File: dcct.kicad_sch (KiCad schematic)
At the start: 0 parts

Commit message: Add DCCT ADCs
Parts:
- added C147, C153, C154, C155, C156, C157, C160, C161, C162, C166, C171, C172, C178, C180: 10uF, Capacitor_SMD:C_0603_1608Metric, symbol Device:C_Small
- added C148, C152, C158, C163, C164, C165, C170, C173, C174, C179, C181: 0.1uF, Capacitor_SMD:C_0402_1005Metric, symbol Device:C_Small
- added C149, C150, C167, C169, C175, C177: 6800pF, Capacitor_SMD:C_0402_1005Metric, symbol Device:C_Small
- added C151, C168, C176: 3300pF, Capacitor_SMD:C_0402_1005Metric, symbol Device:C_Small
- added C159: 0.01uF, Capacitor_SMD:C_0402_1005Metric, symbol Device:C_Small
- added R54, R55: 1.0K, Resistor_SMD:R_0402_1005Metric, symbol Device:R_US
- added R56: 665, Resistor_SMD:R_0402_1005Metric, symbol Device:R_US
- added R57: 0, Resistor_SMD:R_0402_1005Metric, symbol Device:R_US
- added R58: 1.3K, Resistor_SMD:R_0402_1005Metric, symbol Device:R_US
- added R59, R60: 10K, Resistor_SMD:R_0402_1005Metric, symbol Device:R_US
- added R61, R62: 10, Resistor_SMD:R_0402_1005Metric, symbol Device:R_US
- added R63: 15, Resistor_SMD:R_0402_1005Metric, symbol Device:R_US
- added R64, R65: 30.1, Resistor_SMD:R_0402_1005Metric, symbol Device:R_US
- added U32: LTC6655BHLS8-5, myparts:LTC6655, symbol PSC:LTC6655BHLS8-5
- added U33: AD8429BRZ, myparts:SOIC127P600X175-8N, symbol Amplifier_Instrumentation:AD8429BRZ
- added U34: AD8675ARZ, Package_SO:SOIC-8_3.9x4.9mm_P1.27mm, symbol PSC:AD8675ARZ
- added U35: LT6202CS5, myparts:LT6202CS5, symbol PSC:LT6202CS5
- added U36: LTC6363xMS8, Package_SO:MSOP-8_3x3mm_P0.65mm, symbol PSC:LTC6363xMS8
- added U37: LTC2376CDE-20-PBF, DFN-16_DE_LIT, symbol PSC:LTC2376CDE-20-PBF
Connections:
- new net: C176.2, C177.1, R65.1, U37.4 (IN+)
- new net: R65.2, U36.4 (+)
- new net: C160.1, R59.1, R60.1, U35.3 (+)
- new net: C168.2, C169.1, R63.1, U36.1 (-)
- new net: C166.1, C170.1, R61.1, U36.2 (VOCM)
- new net: R64.2, U36.5 (-)
- new net: C167.2, C168.1, R62.1, U36.8 (+)
- new net: C155.1, C157.1, R57.1, R59.2, U37.7 (REF), U37.8 (REF/*DGC)
- new net: C153.1, R57.2, U32.6 (VOUT_S), U32.7 (VOUT_F)
- new net: R61.2, U35.1, U35.4 (-)
- new net: R62.2, U34.2 (-), U34.6
- new net: C159.1, R58.1, U34.3 (+)
- new net: C175.2, C176.1, R64.1, U37.5 (IN-)
- new net: C149.2, C151.1, R54.1, U33.1 (-)
- new net: C150.1, C151.2, R55.1, U33.4 (+)
- new net: R58.2, U33.7
- new net: R56.1, U33.2 (Rg)
- new net: R56.2, U33.3 (Rg)
- new net +1.8V: C180.1, C181.1, U37.15 (OVDD)
- new net +10V: C147.1, C148.1, U32.1 (IN), U32.2 (~SHDN)
- new net +15V: C156.1, C158.1, C162.1, C165.1, U33.8 (Vs+), U34.7 (V+)
- new net +2.5V: C178.1, C179.1, U37.2 (VDD)
- new net +5.3VA: C164.1, C171.1, C173.1, U35.5 (V+), U36.3 (V+)
- new net -15V: C152.1, C154.1, C161.1, C163.1, U33.5 (Vs-), U34.4 (V-)
- new net -5.3VA: C172.1, C174.1, U36.6 (V-)
- new net GND: C147.2, C148.2, C149.1, C150.2, C152.2, C153.2, C154.2, C155.2, C156.2, C157.2, C158.2, C159.2, C160.2, C161.2, C162.2, C163.2, C164.2, C165.2, C166.2, C167.1, C169.2, C170.2, C171.2, C172.2, C173.2, C174.2, C175.1, C177.2, C178.2, C179.2, C180.2, C181.2, R60.2, R63.2, U32.3 (GND), U32.4 (GND), U32.5 (GND), U32.8 (GND), U33.6 (Ref), U35.2 (V-), U37.1 (CHAIN), U37.10 (GND), U37.12 (RDL/SDI), U37.16 (GND), U37.17 (GND), U37.3 (GND), U37.6 (GND)
- new net busy: U37.11 (BUSY)
- new net cnv: U37.9 (CNV)
- new net dcct+: R55.2
- new net dcct-: R54.2
- new net sck: U37.13 (SCK)
- new net sdo: U37.14 (SDO)
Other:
- note added: "Add TVS SP3118-01ETG"

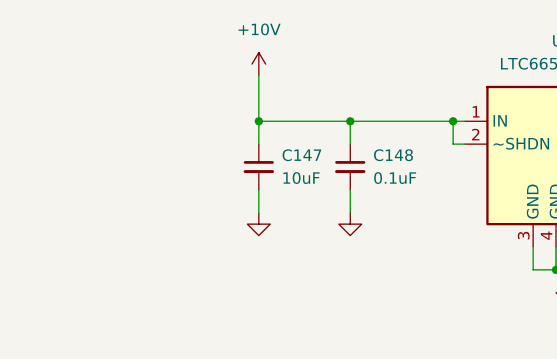
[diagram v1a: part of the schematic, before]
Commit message: DAC and DCCT placement
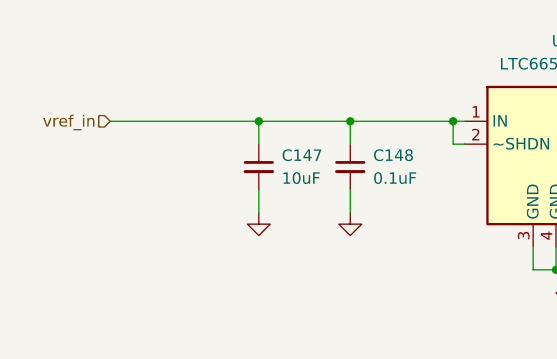
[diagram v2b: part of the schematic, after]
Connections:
- net +10V renamed vref_in
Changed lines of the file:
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@@
 	)
 	(junction
+		(at 53.34 35.56)
+		(diameter 0)
+		(color 0 0 0 0)
+	)
+	(junction
 		(at 365.76 128.27)
 		(diameter 0)
@@
 	)
 	(junction
-		(at 53.34 35.56)
-		(diameter 0)
-		(color 0 0 0 0)
-	)
-	(junction
 		(at 241.3 95.25)
 		(diameter 0)
@@
 	(wire
 		(pts
-			(xy 53.34 30.48) (xy 53.34 35.56)
-		)
-		(stroke
-			(width 0)
-			(type default)
-		)
-	)
-	(wire
-		(pts
 			(xy 71.12 118.11) (xy 71.12 120.65)
 		)
@@
 	(wire
 		(pts
+			(xy 36.83 35.56) (xy 53.34 35.56)
+		)
+		(stroke
+			(width 0)
+			(type default)
+		)
+	)
+	(wire
+		(pts
 			(xy 241.3 147.32) (xy 241.3 146.05)
 		)
@@
 		)
 	)
+	(hierarchical_label "vref_in"
+		(shape input)
+		(at 36.83 35.56 180)
+		(effects
+			(font
+				(size 1.27 1.27)
+			)
+			(justify right)
+		)
+	)
 	(symbol
 		(lib_id "power:GND")
@@
 					(unit 1)
 				)
-			)
-		)
-	)
-	(symbol
-		(lib_id "power:+10V")
-		(at 53.34 30.48 0)
-		(unit 1)
-		(exclude_from_sim no)
-		(in_bom yes)
-		(on_board yes)
-		(dnp no)
-		(fields_autoplaced yes)
-		(property "Reference" "#PWR0215"
-			(at 53.34 34.29 0)
-			(effects
-				(font
-					(size 1.27 1.27)
-				)
-				(hide yes)
-			)
-		)
-		(property "Value" "+10V"
-			(at 53.34 25.4 0)
-			(effects
-				(font
-					(size 1.27 1.27)
-				)
-			)
-		)
-		(property "Footprint" ""
-			(at 53.34 30.48 0)
-			(effects
-				(font
-					(size 1.27 1.27)
-				)
-				(hide yes)
-			)
-		)
-		(property "Datasheet" ""
-			(at 53.34 30.48 0)
-			(effects
-				(font
-					(size 1.27 1.27)
-				)
-				(hide yes)
-			)
-		)
-		(property "Description" "Power symbol creates a global label with name \"+10V\""
-			(at 53.34 30.48 0)
-			(effects
-				(font
-					(size 1.27 1.27)
-				)
-				(hide yes)
-			)
-		)
-		(pin "1"
-		)
-		(instances
-			(project "psc_daughter_brd"
-				(path "/40891cc8-bf64-41f4-8f69-a607d7b280eb/befff6ff-020c-4bdc-a736-6c19d2d39203/01b24c67-d057-4790-88f6-07e11ed5cbc3"
-					(reference "#PWR0168")
-					(unit 1)
-				)
-				(path "/40891cc8-bf64-41f4-8f69-a607d7b280eb/befff6ff-020c-4bdc-a736-6c19d2d39203/e462b81c-c1ec-4974-a851-a02502e296f2"
-					(reference "#PWR0215")
-					(unit 1)
-				)

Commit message: finish rough placement
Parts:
- removed C147, C153, C155, C157, C160, C166: 10uF, Capacitor_SMD:C_0603_1608Metric, symbol Device:C_Small
- removed C148, C164, C170: 0.1uF, Capacitor_SMD:C_0402_1005Metric, symbol Device:C_Small
- removed R57: 0, Resistor_SMD:R_0402_1005Metric, symbol Device:R_US
- removed R59, R60: 10K, Resistor_SMD:R_0402_1005Metric, symbol Device:R_US
- removed R61: 10, Resistor_SMD:R_0402_1005Metric, symbol Device:R_US
- removed U32: LTC6655BHLS8-5, myparts:LTC6655, symbol PSC:LTC6655BHLS8-5
- removed U35: LT6202CS5, myparts:LT6202CS5, symbol PSC:LT6202CS5
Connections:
- net drv_vref: now reaches U36.2 (VOCM)
- net adc_vref: now reaches U37.7 (REF), U37.8 (REF/*DGC)

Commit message: Tweaks to connector pinouts
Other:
- note added: "Replace with ADA4945-1"
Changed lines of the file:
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@@
+		)
+	)
+	(text "Replace with ADA4945-1"
+		(exclude_from_sim no)
+		(at 255.524 127.762 0)
+		(effects
+			(font
+				(size 1.27 1.27)
+			)
 		)
 	)

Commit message: Finish layout
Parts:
- removed C149, C150: 6800pF, Capacitor_SMD:C_0402_1005Metric, symbol Device:C_Small
- removed R56: 665, Resistor_SMD:R_0402_1005Metric, symbol Device:R_US
- added C35: 2200pF, myparts:EMCT101W222M1GV001E, symbol PSC:EMCT101W222M1GV001E
- added D4: SP3118-01ETG, myparts:sp3118-01etg, symbol PSC:SP3118-01ETG
- added R56: 665, Resistor_SMD:R_0603_1608Metric, symbol Device:R_Small_US
- C151, C168, C176: Cost (none) -> .01; MFG (none) -> Samsung; MFG_PN (none) -> CL05B332KB5NNNC
- C152, C158, C163, C165, C173, C174, C179, C181: MFG (none) -> Taiyo Yuden; MFG_PN (none) -> TMK105BJ104KV-F
- C154, C156, C161, C162, C171, C172, C178, C180: MFG (none) -> Samsung; MFG_PN (none) -> CL10A106MA8NRNC
- C159: Cost (none) -> .01; MFG (none) -> Taiyo Yuden; MFG_PN (none) -> MBASU105SB7103KFNA18
- C167, C169, C175, C177: MFG (none) -> Samsung; MFG_PN (none) -> CAP CER 3300PF 50V X7R 0402
- R54, R55: Cost (none) -> .01; MFG (none) -> Panasonic; MFG_PN (none) -> ERJ-2RKF1001X; Tolerance 0.1% -> 1%
- R58: Cost (none) -> .01; MFG (none) -> Panasonic; MFG_PN (none) -> ERJ-2RKF1301X
- R62: Cost (none) -> .01; MFG (none) -> Panasonic; MFG_PN (none) -> ERJ-2RKF10R0X
- R63: Cost (none) -> .01; MFG (none) -> Panasonic; MFG_PN (none) -> ERJ-2RKF15R0X
- R64, R65: Cost (none) -> .01; MFG (none) -> Panasonic; MFG_PN (none) -> ERJ-2RKF30R1X
- U33: Cost (none) -> 12.76; MFG (none) -> Analog Devices; MFG_PN (none) -> AD8429BRZ
- U34: Cost (none) -> 2.88; MFG (none) -> Analog Devices; MFG_PN (none) -> AD8675ARZ
- U36: value LTC6363xMS8 -> LTC6363IMS8; Cost (none) -> 7.61; MFG (none) -> Analog Devices; MFG_PN (none) -> LTC6363IMS8#TRPBF
- U37: value LTC2376CDE-20-PBF -> LTC2376CDE-20; Cost (none) -> 34.72; MFG (none) -> Analog Devices; MFG_PN (none) -> LTC2376CDE-20#PBF
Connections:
- net GND: now also C35.3, C35.4
- net at C176.2, C177.1, R65.1: now also U37.5 (IN-); no longer U37.4 (IN+)
- net at C175.2, C176.1, R64.1: now also U37.4 (IN+); no longer U37.5 (IN-)
- net at C151.1, R54.1, U33.1 (-): now also C35.1, D4.2 (A2)
- net at C151.2, R55.1, U33.4 (+): now also C35.2, D4.1 (A1)
- net at U33.2 (Rg): now also R56.1
- net at U33.3 (Rg): now also R56.2
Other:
- note removed: "Add TVS SP3118-01ETG"
- moved on the sheet: C151, R54, R55
